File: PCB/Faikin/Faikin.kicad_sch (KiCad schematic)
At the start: 47 parts, among them J1 1x5, J2 TC2030-USB-NL, J3 Reset, Q1 BSS138PS, U1 TPS562246, U4 ESP32-S3-MINI-1

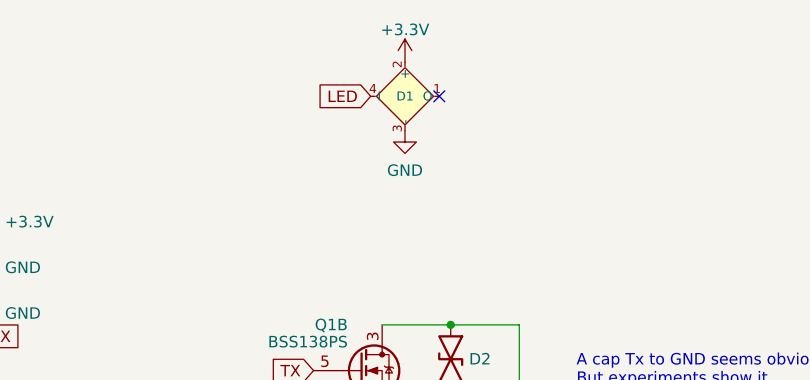
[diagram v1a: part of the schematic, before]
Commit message: Rework with new LED and TC2030 rotate
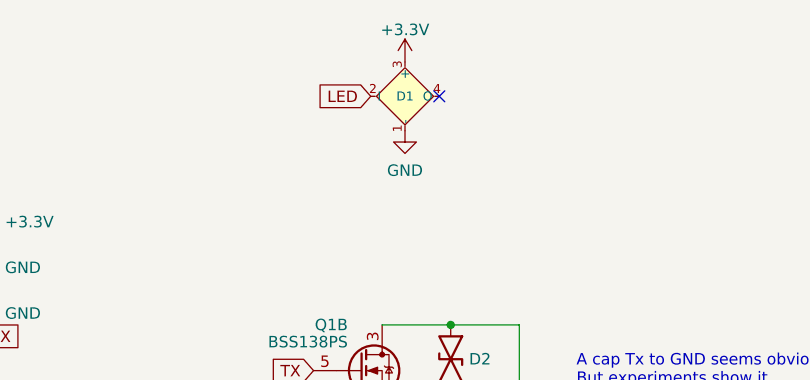
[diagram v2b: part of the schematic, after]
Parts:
- D1: value XL-1010RGBC-WS2812B -> XL-1516RGBC-WS2812B; footprint RevK:SMD1010 -> RevK:SMD1615; symbol RevK:WS2812B-1mm -> RevK:WS2812B-1.5mm; MPN C5349953 -> C5349954
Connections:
- net +3.3V: now also D1.3 (+); no longer D1.2 (+)
- net GND: now also D1.1 (-); no longer D1.3 (-)
- net LED: now also D1.2 (I); no longer D1.4 (I)
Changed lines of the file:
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@@
 			)
 		)
-		(property "Sim.Enable" "0"
-			(at 262.255 170.815 0)
-			(effects
-				(font
-					(size 1.27 1.27)
-				)
-				(hide yes)
-			)
-		)
 		(instances
 			(project "Faikin"
@@
 			)
 		)
-		(property "Sim.Enable" "0"
-			(at 259.08 173.99 0)
-			(effects
-				(font
-					(size 1.27 1.27)
-				)
-				(hide yes)
-			)
-		)
 		(instances
 			(project "Faikin"
@@
 			)
 		)
-		(property "Sim.Enable" "0"
-			(at 262.255 177.165 0)
-			(effects
-				(font
-					(size 1.27 1.27)
-				)
-				(hide yes)
-			)
-		)
 		(instances
 			(project "Faikin"
@@
 			)
 		)
-		(property "Sim.Enable" "0"
-			(at 262.255 176.53 0)
-			(effects
-				(font
-					(size 1.27 1.27)
-				)
-				(hide yes)
-			)
-		)
 		(instances
 			(project "Faikin"
@@
 			)
 		)
-		(property "Sim.Enable" "0"
-			(at 265.43 173.99 0)
-			(effects
-				(font
-					(size 1.27 1.27)
-				)
-				(hide yes)
-			)
-		)
 		(instances
 			(project "Faikin"
@@
 			)
 		)
-		(property "Sim.Enable" "0"
-			(at 262.255 171.45 0)
-			(effects
-				(font
-					(size 1.27 1.27)
-				)
-				(hide yes)
-			)
-		)
 		(instances
 			(project "Faikin"
@@
 	)
 	(symbol
-		(lib_id "RevK:WS2812B-1mm")
+		(lib_id "RevK:WS2812B-1.5mm")
 		(at 161.925 46.355 0)
 		(unit 1)
@@
 			)
 		)
-		(property "Value" "XL-1010RGBC-WS2812B"
+		(property "Value" "XL-1516RGBC-WS2812B"
 			(at 163.195 52.07 0)
 			(effects
@@
 			)
 		)
-		(property "Footprint" "RevK:SMD1010"
-			(at 163.195 53.975 0)
+		(property "Footprint" "RevK:SMD1615"
+			(at 163.195 38.735 0)
 			(effects
 				(font
@@
 		)
 		(property "Datasheet" "https://datasheet.lcsc.com/lcsc/2301111010_XINGLIGHT-XL-1010RGBC-WS2812B_C5349953.pdf"
-			(at 163.195 55.88 0)
+			(at 163.195 36.83 0)
 			(effects
 				(font
@@
 			)
 		)
-		(property "MPN" "C5349953"
-			(at 163.195 57.785 0)
+		(property "MPN" "C5349954"
+			(at 163.195 34.925 0)
 			(effects
 				(font

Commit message: Minor tweaks
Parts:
- D1: footprint RevK:SMD1615 -> RevK:SMD1615-Blind
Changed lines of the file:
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@@
 			)
 		)
-		(property "Footprint" "RevK:SMD1615"
+		(property "Footprint" "RevK:SMD1615-Blind"
 			(at 163.195 38.735 0)
 			(effects

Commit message: Library update
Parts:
- C15: value 47uF 6V -> 47uF 6V3
- D1: value XL-1516RGBC-WS2812B -> XL-1615RGBC-2812B
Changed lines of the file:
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@@
 			)
 		)
-		(property "Value" "47uF 6V"
+		(property "Value" "47uF 6V3"
 			(at 123.317 179.07 0)
 			(effects
@@
 			)
 		)
-		(property "Value" "XL-1516RGBC-WS2812B"
+		(property "Value" "XL-1615RGBC-2812B"
 			(at 163.195 52.07 0)
 			(effects
@@
 			)
 		)
-		(property "Datasheet" "https://datasheet.lcsc.com/lcsc/2301111010_XINGLIGHT-XL-1010RGBC-WS2812B_C5349953.pdf"
+		(property "Datasheet" "https://www.lcsc.com/datasheet/C5349954.pdf"
 			(at 163.195 36.83 0)
 			(effects

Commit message: Minor tweaks
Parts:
- D1: footprint RevK:SMD1615-Blind -> RevK:SMD1615
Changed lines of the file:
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@@
 			)
 		)
-		(property "Footprint" "RevK:SMD1615-Blind"
+		(property "Footprint" "RevK:SMD1615"
 			(at 163.195 38.735 0)
 			(effects
